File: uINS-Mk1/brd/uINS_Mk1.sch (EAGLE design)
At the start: 13 parts

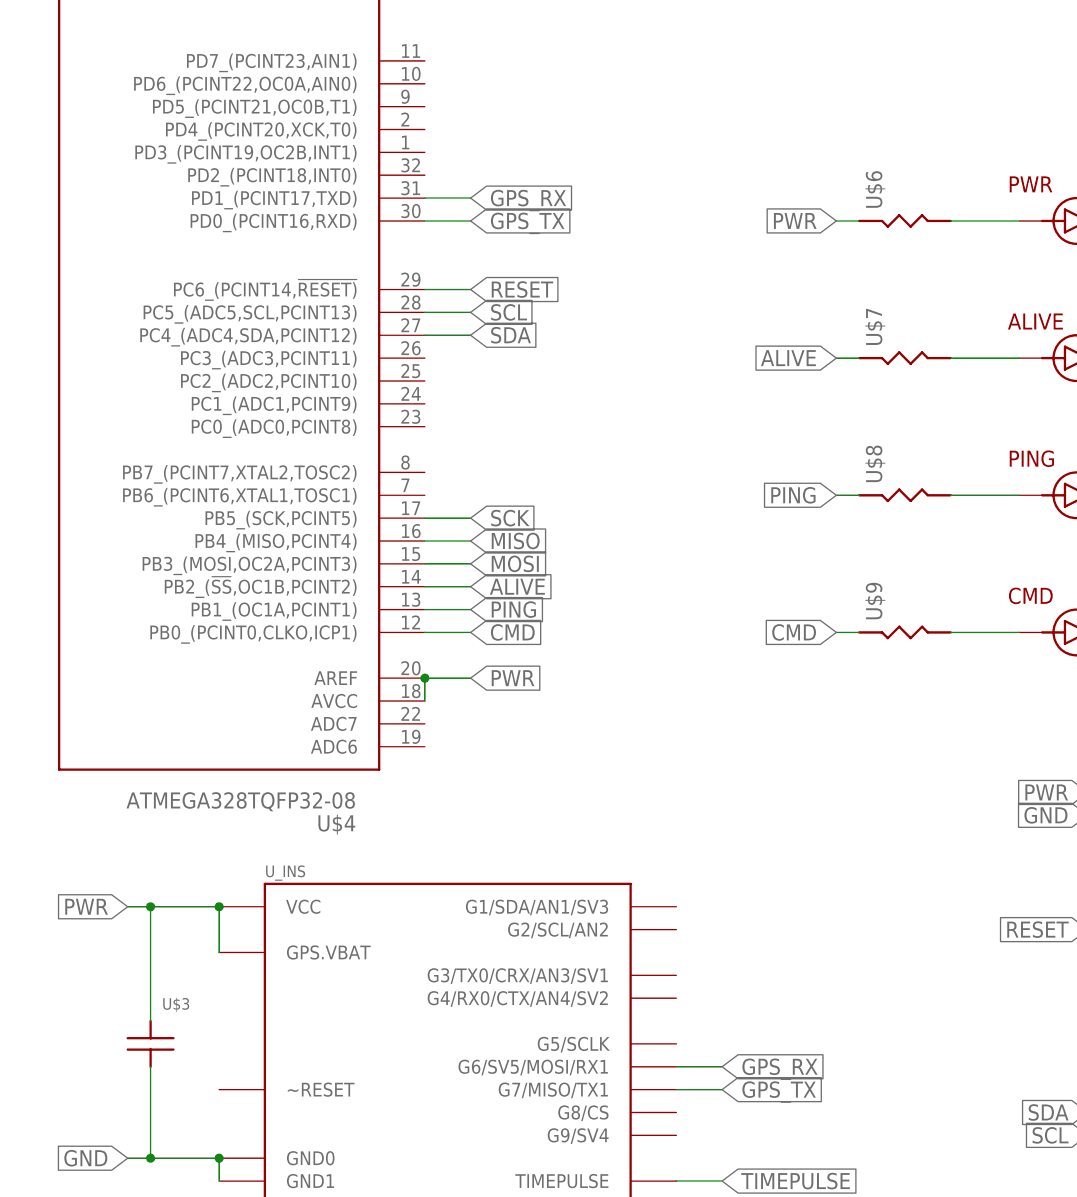
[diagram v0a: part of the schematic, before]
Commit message: updated board templates and modified existing boards to use the mk2 templates.
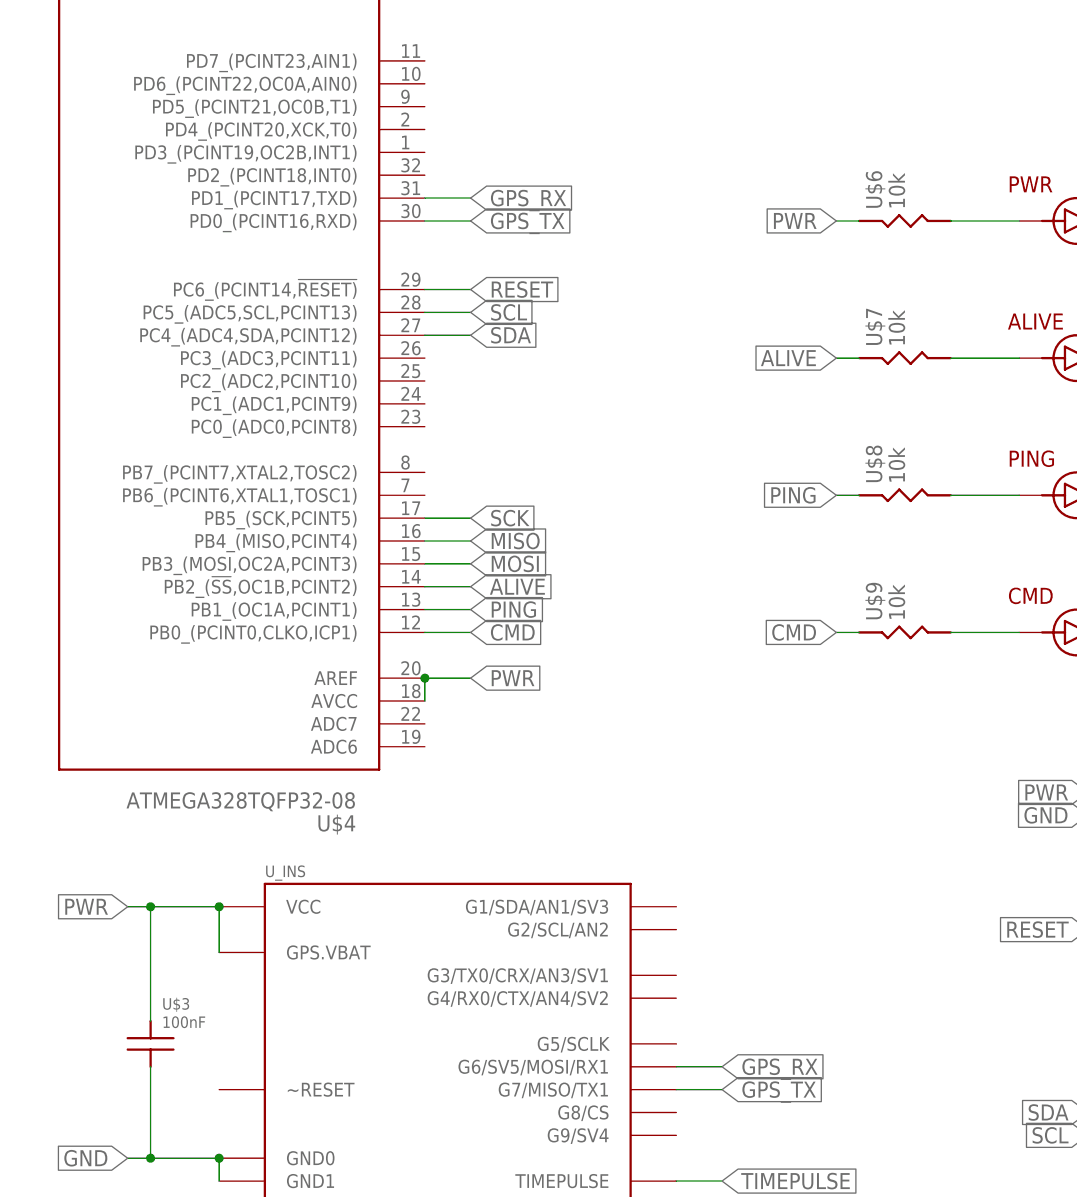
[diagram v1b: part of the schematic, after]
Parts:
- U$3: value (none) -> 100nF
- U$6, U$7, U$8, U$9: value (none) -> 10k
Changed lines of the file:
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@@
 <?xml version="1.0" encoding="utf-8"?>
 <!DOCTYPE eagle SYSTEM "eagle.dtd">
-<eagle version="8.2.2">
+<eagle version="8.3.1">
 <drawing>
 <settings>
 <setting alwaysvectorfont="no"/>
+<setting keepoldvectorfont="yes"/>
 <setting verticaltext="up"/>
 </settings>
@@
 <layer number="97" name="Info" color="7" fill="1" visible="yes" active="yes"/>
 <layer number="98" name="Guide" color="6" fill="1" visible="yes" active="yes"/>
+<layer number="99" name="SpiceOrder" color="5" fill="1" visible="yes" active="yes"/>
 <layer number="100" name="Muster" color="7" fill="1" visible="no" active="no"/>
 <layer number="101" name="Patch_Top" color="12" fill="4" visible="no" active="yes"/>
@@
 <part name="U$1" library="000_CustomPartsMaster" deviceset="SENSOR_MODULE_MK1" device=""/>
 <part name="U_INS" library="000_CustomPartsMaster" deviceset="U_INS" device=""/>
-<part name="U$3" library="000_CustomPartsMaster" deviceset="CAPACITOR-UNPOLARIZED" device="0805"/>
+<part name="U$3" library="000_CustomPartsMaster" deviceset="CAPACITOR-UNPOLARIZED" device="0805" value="100nF"/>
 <part name="U$4" library="000_CustomPartsMaster" deviceset="ATMEGA328" device="TQFP32-08"/>
 <part name="U$5" library="000_CustomPartsMaster" deviceset="6PIN-HEADER" device="2X3"/>
-<part name="U$6" library="000_CustomPartsMaster" deviceset="RESISTOR" device=""/>
-<part name="U$7" library="000_CustomPartsMaster" deviceset="RESISTOR" device=""/>
-<part name="U$8" library="000_CustomPartsMaster" deviceset="RESISTOR" device=""/>
-<part name="U$9" library="000_CustomPartsMaster" deviceset="RESISTOR" device=""/>
+<part name="U$6" library="000_CustomPartsMaster" deviceset="RESISTOR" device="" value="10k"/>
+<part name="U$7" library="000_CustomPartsMaster" deviceset="RESISTOR" device="" value="10k"/>
+<part name="U$8" library="000_CustomPartsMaster" deviceset="RESISTOR" device="" value="10k"/>
+<part name="U$9" library="000_CustomPartsMaster" deviceset="RESISTOR" device="" value="10k"/>
 <part name="U$10" library="000_CustomPartsMaster" deviceset="RESISTOR" device=""/>
 <part name="U$11" library="000_CustomPartsMaster" deviceset="CAPACITOR-UNPOLARIZED" device="0805"/>
